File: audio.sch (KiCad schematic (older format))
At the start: 22 parts

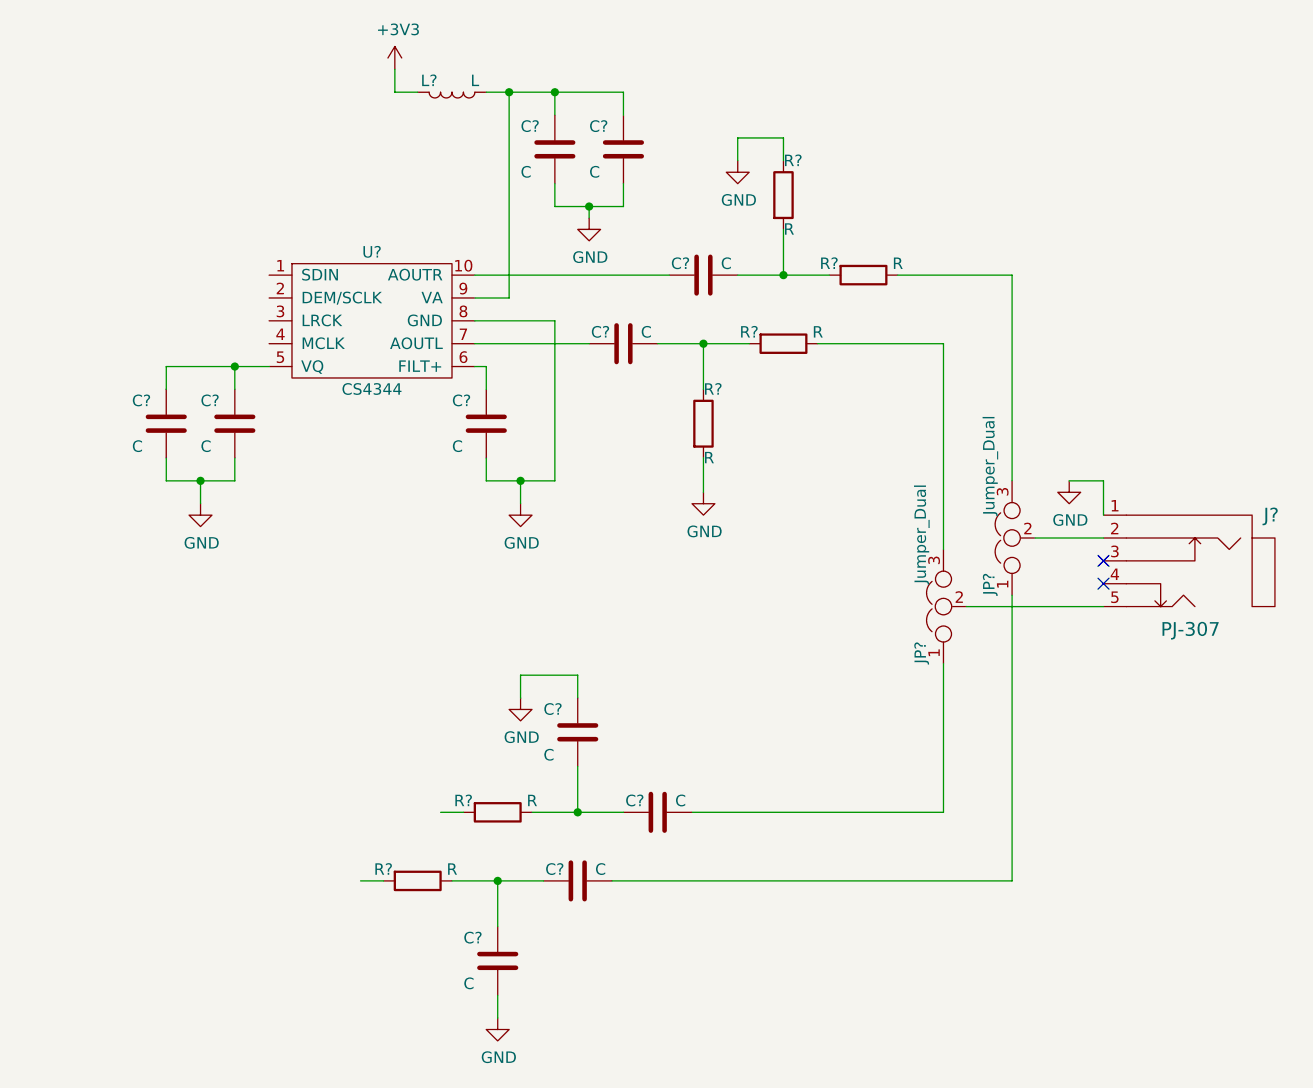
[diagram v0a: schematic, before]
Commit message: HDMI and VGA circuit added.
Signed-off-by: Kali Prasad <kprasadvnsi@protonmail.com>
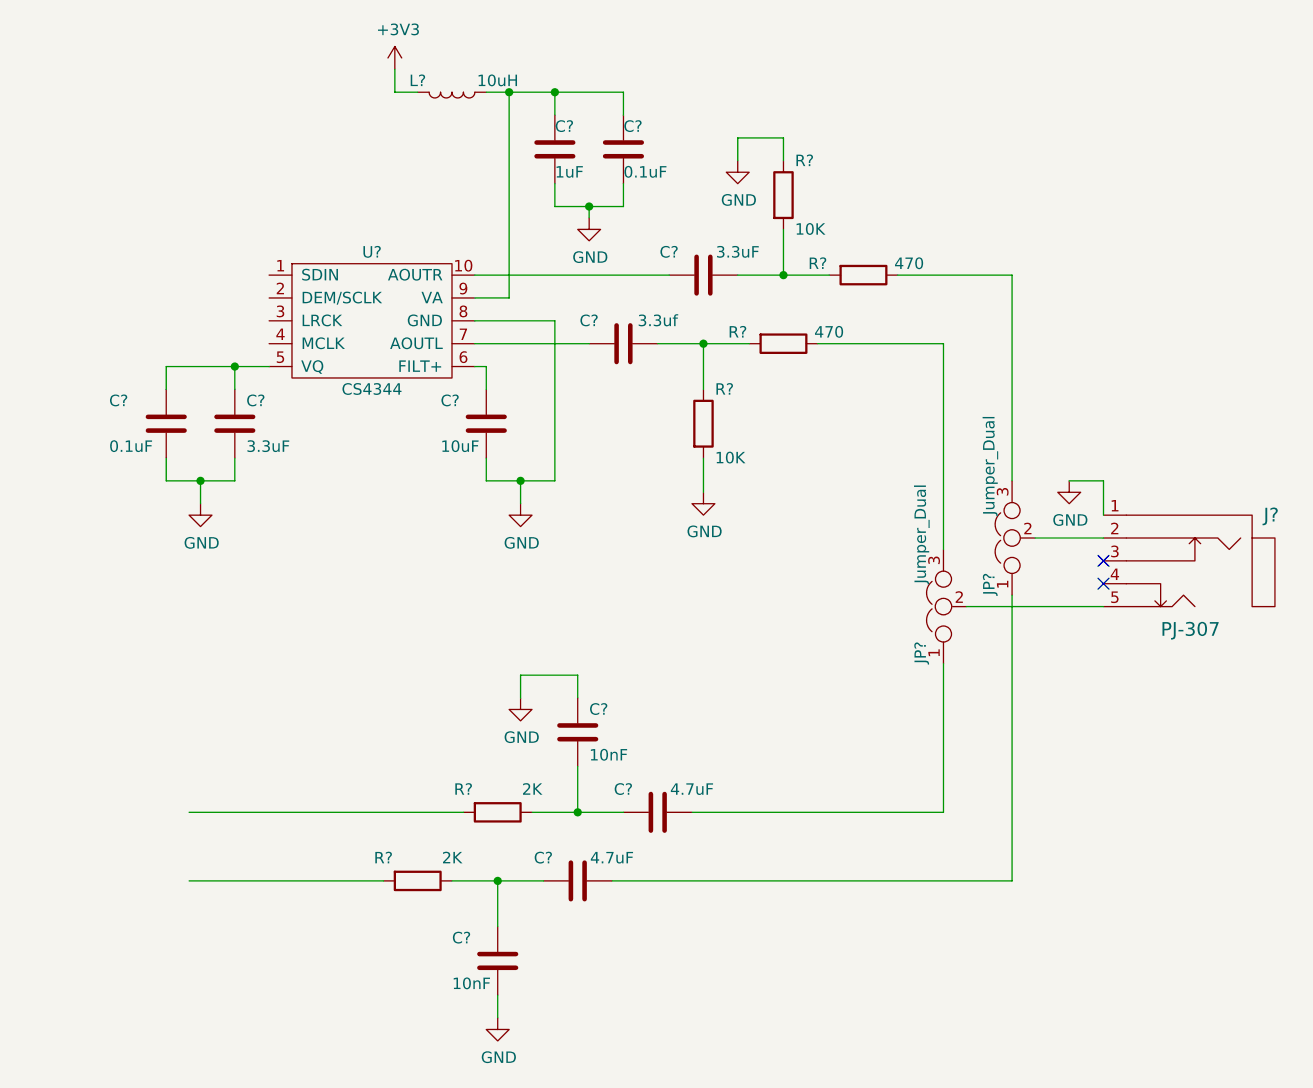
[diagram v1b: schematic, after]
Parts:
- C?: value C -> 3.3uf
- C? (x2): value C -> 3.3uF
- C?: value C -> 10uF
- C? (x2): value C -> 0.1uF
- C?: value C -> 1uF
- C? (x2): value C -> 4.7uF
- C? (x2): value C -> 10nF
- L?: value L -> 10uH
- R? (x2): value R -> 10K
- R? (x2): value R -> 470
- R? (x2): value R -> 2K
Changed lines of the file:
@@
 U 1 1 5D08C7BA
 P 4950 2700
-F 0 "C?" V 4900 2600 50  0000 C CNN
-F 1 "C" V 4900 2800 50  0000 C CNN
+F 0 "C?" V 4850 2550 50  0000 C CNN
+F 1 "3.3uf" V 4850 2850 50  0000 C CNN
 F 2 "" H 4988 2550 50  0001 C CNN
 F 3 "~" H 4950 2700 50  0001 C CNN
@@
 U 1 1 5D08EF53
 P 5300 3050
-F 0 "R?" H 5300 3200 50  0000 L CNN
-F 1 "R" H 5300 2900 50  0000 L CNN
+F 0 "R?" H 5350 3200 50  0000 L CNN
+F 1 "10K" H 5350 2900 50  0000 L CNN
 F 2 "" V 5230 3050 50  0001 C CNN
 F 3 "~" H 5300 3050 50  0001 C CNN
@@
 U 1 1 5D08F5D6
 P 5650 2700
-F 0 "R?" V 5600 2550 50  0000 C CNN
-F 1 "R" V 5600 2850 50  0000 C CNN
+F 0 "R?" V 5600 2500 50  0000 C CNN
+F 1 "470" V 5600 2900 50  0000 C CNN
 F 2 "" V 5580 2700 50  0001 C CNN
 F 3 "~" H 5650 2700 50  0001 C CNN
@@
 U 1 1 5D092BC6
 P 5300 2400
-F 0 "C?" V 5250 2300 50  0000 C CNN
-F 1 "C" V 5250 2500 50  0000 C CNN
+F 0 "C?" V 5200 2250 50  0000 C CNN
+F 1 "3.3uF" V 5200 2550 50  0000 C CNN
 F 2 "" H 5338 2250 50  0001 C CNN
 F 3 "~" H 5300 2400 50  0001 C CNN
@@
 U 1 1 5D09362D
 P 6000 2400
-F 0 "R?" V 5950 2250 50  0000 C CNN
-F 1 "R" V 5950 2550 50  0000 C CNN
+F 0 "R?" V 5950 2200 50  0000 C CNN
+F 1 "470" V 5950 2600 50  0000 C CNN
 F 2 "" V 5930 2400 50  0001 C CNN
 F 3 "~" H 6000 2400 50  0001 C CNN
@@
 U 1 1 5D09A828
 P 5650 2050
-F 0 "R?" H 5650 2200 50  0000 L CNN
-F 1 "R" H 5650 1900 50  0000 L CNN
+F 0 "R?" H 5700 2200 50  0000 L CNN
+F 1 "10K" H 5700 1900 50  0000 L CNN
 F 2 "" V 5580 2050 50  0001 C CNN
 F 3 "~" H 5650 2050 50  0001 C CNN
@@
 U 1 1 5D0A15AD
 P 4350 3050
-F 0 "C?" H 4200 3150 50  0000 L CNN
-F 1 "C" H 4200 2950 50  0000 L CNN
+F 0 "C?" H 4150 3150 50  0000 L CNN
+F 1 "10uF" H 4150 2950 50  0000 L CNN
 F 2 "" H 4388 2900 50  0001 C CNN
 F 3 "~" H 4350 3050 50  0001 C CNN
@@
 U 1 1 5D0DA66D
 P 4200 1600
-F 0 "L?" V 4150 1500 50  0000 C CNN
-F 1 "L" V 4150 1700 50  0000 C CNN
+F 0 "L?" V 4150 1450 50  0000 C CNN
+F 1 "10uH" V 4150 1800 50  0000 C CNN
 F 2 "" H 4200 1600 50  0001 C CNN
 F 3 "~" H 4200 1600 50  0001 C CNN
@@
 U 1 1 5D306893
 P 4650 1850
-F 0 "C?" H 4500 1950 50  0000 L CNN
-F 1 "C" H 4500 1750 50  0000 L CNN
+F 0 "C?" H 4650 1950 50  0000 L CNN
+F 1 "1uF" H 4650 1750 50  0000 L CNN
 F 2 "" H 4688 1700 50  0001 C CNN
 F 3 "~" H 4650 1850 50  0001 C CNN
@@
 U 1 1 5D30615A
 P 4950 1850
-F 0 "C?" H 4800 1950 50  0000 L CNN
-F 1 "C" H 4800 1750 50  0000 L CNN
+F 0 "C?" H 4950 1950 50  0000 L CNN
+F 1 "0.1uF" H 4950 1750 50  0000 L CNN
 F 2 "" H 4988 1700 50  0001 C CNN
 F 3 "~" H 4950 1850 50  0001 C CNN
@@
 U 1 1 5D36B321
 P 4050 5050
-F 0 "R?" V 4000 4900 50  0000 C CNN
-F 1 "R" V 4000 5200 50  0000 C CNN
+F 0 "R?" V 3950 4900 50  0000 C CNN
+F 1 "2K" V 3950 5200 50  0000 C CNN
 F 2 "" V 3980 5050 50  0001 C CNN
 F 3 "~" H 4050 5050 50  0001 C CNN
@@
 U 1 1 5D36BD4D
 P 4750 5050
-F 0 "C?" V 4700 4950 50  0000 C CNN
-F 1 "C" V 4700 5150 50  0000 C CNN
+F 0 "C?" V 4650 4900 50  0000 C CNN
+F 1 "4.7uF" V 4650 5200 50  0000 C CNN
 F 2 "" H 4788 4900 50  0001 C CNN
 F 3 "~" H 4750 5050 50  0001 C CNN
@@
 U 1 1 5D36C27B
 P 4400 5400
-F 0 "C?" H 4250 5500 50  0000 L CNN
-F 1 "C" H 4250 5300 50  0000 L CNN
+F 0 "C?" H 4200 5500 50  0000 L CNN
+F 1 "10nF" H 4200 5300 50  0000 L CNN
 F 2 "" H 4438 5250 50  0001 C CNN
 F 3 "~" H 4400 5400 50  0001 C CNN
@@
 	1    0    0    -1
 $EndComp
-Wire Wire Line
-	3900 5050 3800 5050
 $Comp
 L Device:R R?
 U 1 1 5D3792B3
 P 4400 4750
-F 0 "R?" V 4350 4600 50  0000 C CNN
-F 1 "R" V 4350 4900 50  0000 C CNN
+F 0 "R?" V 4300 4600 50  0000 C CNN
+F 1 "2K" V 4300 4900 50  0000 C CNN
 F 2 "" V 4330 4750 50  0001 C CNN
 F 3 "~" H 4400 4750 50  0001 C CNN
@@
 U 1 1 5D37AB97
 P 4750 4400
-F 0 "C?" H 4600 4500 50  0000 L CNN
-F 1 "C" H 4600 4300 50  0000 L CNN
+F 0 "C?" H 4800 4500 50  0000 L CNN
+F 1 "10nF" H 4800 4300 50  0000 L CNN
 F 2 "" H 4788 4250 50  0001 C CNN
 F 3 "~" H 4750 4400 50  0001 C CNN
@@
 Wire Wire Line
 	4750 4750 4950 4750
-Wire Wire Line
-	4250 4750 4150 4750
 $Comp
 L power:GND #PWR?
@@
 U 1 1 5D37A61B
 P 5100 4750
-F 0 "C?" V 5050 4650 50  0000 C CNN
-F 1 "C" V 5050 4850 50  0000 C CNN
+F 0 "C?" V 5000 4600 50  0000 C CNN
+F 1 "4.7uF" V 5000 4900 50  0000 C CNN
 F 2 "" H 5138 4600 50  0001 C CNN
 F 3 "~" H 5100 4750 50  0001 C CNN
@@
 U 1 1 5D333188
 P 3250 3050
-F 0 "C?" H 3100 3150 50  0000 L CNN
-F 1 "C" H 3100 2950 50  0000 L CNN
+F 0 "C?" H 3300 3150 50  0000 L CNN
+F 1 "3.3uF" H 3300 2950 50  0000 L CNN
 F 2 "" H 3288 2900 50  0001 C CNN
 F 3 "~" H 3250 3050 50  0001 C CNN
@@
 U 1 1 5D3334AD
 P 2950 3050
-F 0 "C?" H 2800 3150 50  0000 L CNN
-F 1 "C" H 2800 2950 50  0000 L CNN
+F 0 "C?" H 2700 3150 50  0000 L CNN
+F 1 "0.1uF" H 2700 2950 50  0000 L CNN
 F 2 "" H 2988 2900 50  0001 C CNN
 F 3 "~" H 2950 3050 50  0001 C CNN
@@
 Wire Wire Line
 	4900 5050 6650 5050
+Wire Wire Line
+	3050 4750 4250 4750
+Wire Wire Line
+	3050 5050 3900 5050
 $EndSCHEMATC

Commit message: SOM added.
Signed-off-by: Kali Prasad <kprasadvnsi@protonmail.com>
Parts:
- C10, C11, C12, C13, C3, C4, C5, C6, C7, C8, C9: renamed from C?; footprint (none) -> Capacitor_SMD:C_0805_2012Metric_Pad1.15x1.40mm_HandSolder
- J5: renamed from J?; footprint (none) -> lt_eval_board:PJ-307
- JP1, JP2: renamed from JP?; footprint (none) -> Jumper:SolderJumper-3_P1.3mm_Bridged12_RoundedPad1.0x1.5mm
- L1: renamed from L?; footprint (none) -> Inductor_SMD:L_0805_2012Metric_Pad1.15x1.40mm_HandSolder
- R54, R55, R56, R57, R58, R59: renamed from R?; footprint (none) -> Resistor_SMD:R_0805_2012Metric_Pad1.15x1.40mm_HandSolder
- gave numbers to parts that had none: 1
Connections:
- net labels added: LRCK, MCLK, SCLK, SDIN
- wire segments 67 -> 71
- no-connect marks 2 -> 4
